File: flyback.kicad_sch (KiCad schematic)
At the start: 17 parts, among them Q1 IPD050N10N5, Q2 IPD050N10N5, T1 MSD1514-103ME

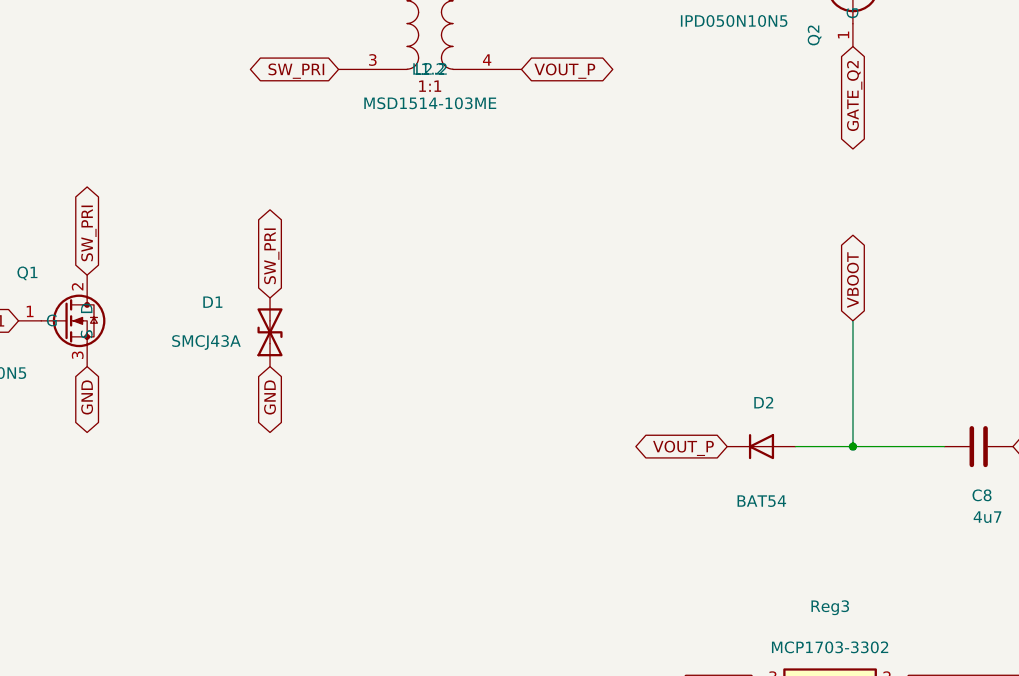
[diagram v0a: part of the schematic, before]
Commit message: Secondaire ISO7710+UCC27517 conservé, ajout retour Vout isolé AMC0311S, modèles 3D
- D2 (bootstrap) remplacé par BAT54C (cathode commune) pour compatibilité pinout
- AMC0311S (U7) ajouté : retour de mesure Vout isolé vers le connecteur C2000
- Connecteur Cpu1 étendu à 8 broches (signaux + masses)
- Correction pastilles Gate/Source sur l'empreinte custom TO-252 (pin1/pin3 inversées)
- Modèles 3D attachés aux empreintes custom (TO-252, MSD1514, A786MW V-chip)
- Image de rendu 3D ajoutée au README

Co-Authored-By: Claude Sonnet 5 <noreply@anthropic.com>
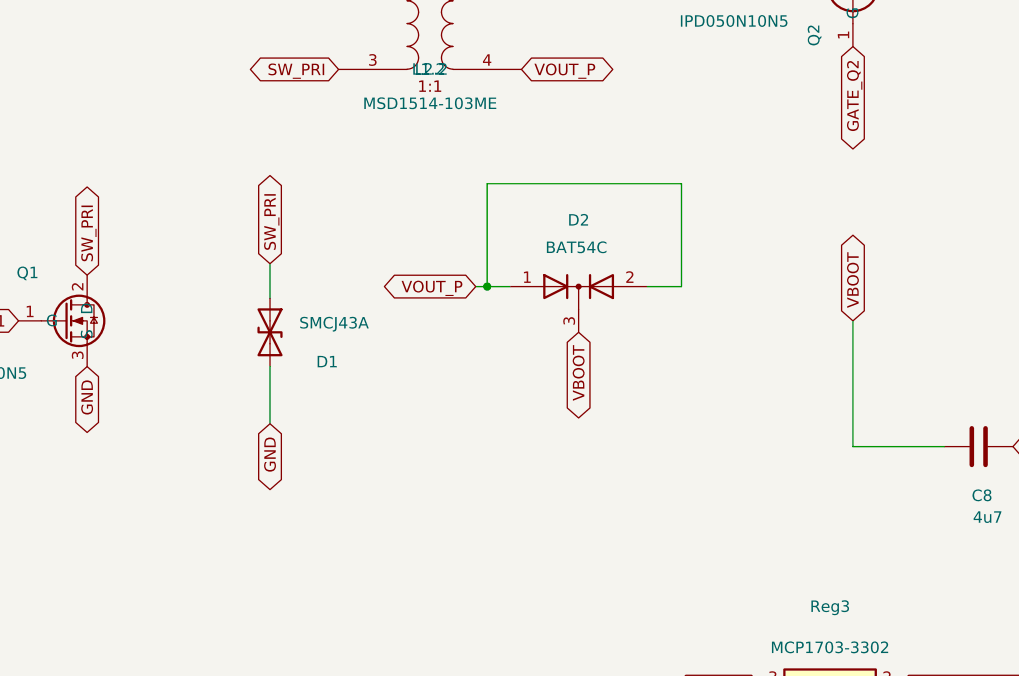
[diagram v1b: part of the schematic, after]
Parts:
- removed D2: BAT54, Diode_SMD:D_SOD-123, symbol Device:D
- added D2: BAT54C, Package_TO_SOT_SMD:SOT-23, symbol Device:D_Dual_CommonCathode_AAK
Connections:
- net GND: now also D1.2 (A2); no longer D1.1 (A1)
- net SW_PRI: now also D1.1 (A1); no longer D1.2 (A2)
- net VBOOT: now also D2.3 (K)
- net VOUT_P: now also D2.1 (A), D2.2 (A)
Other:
- moved on the sheet: D1

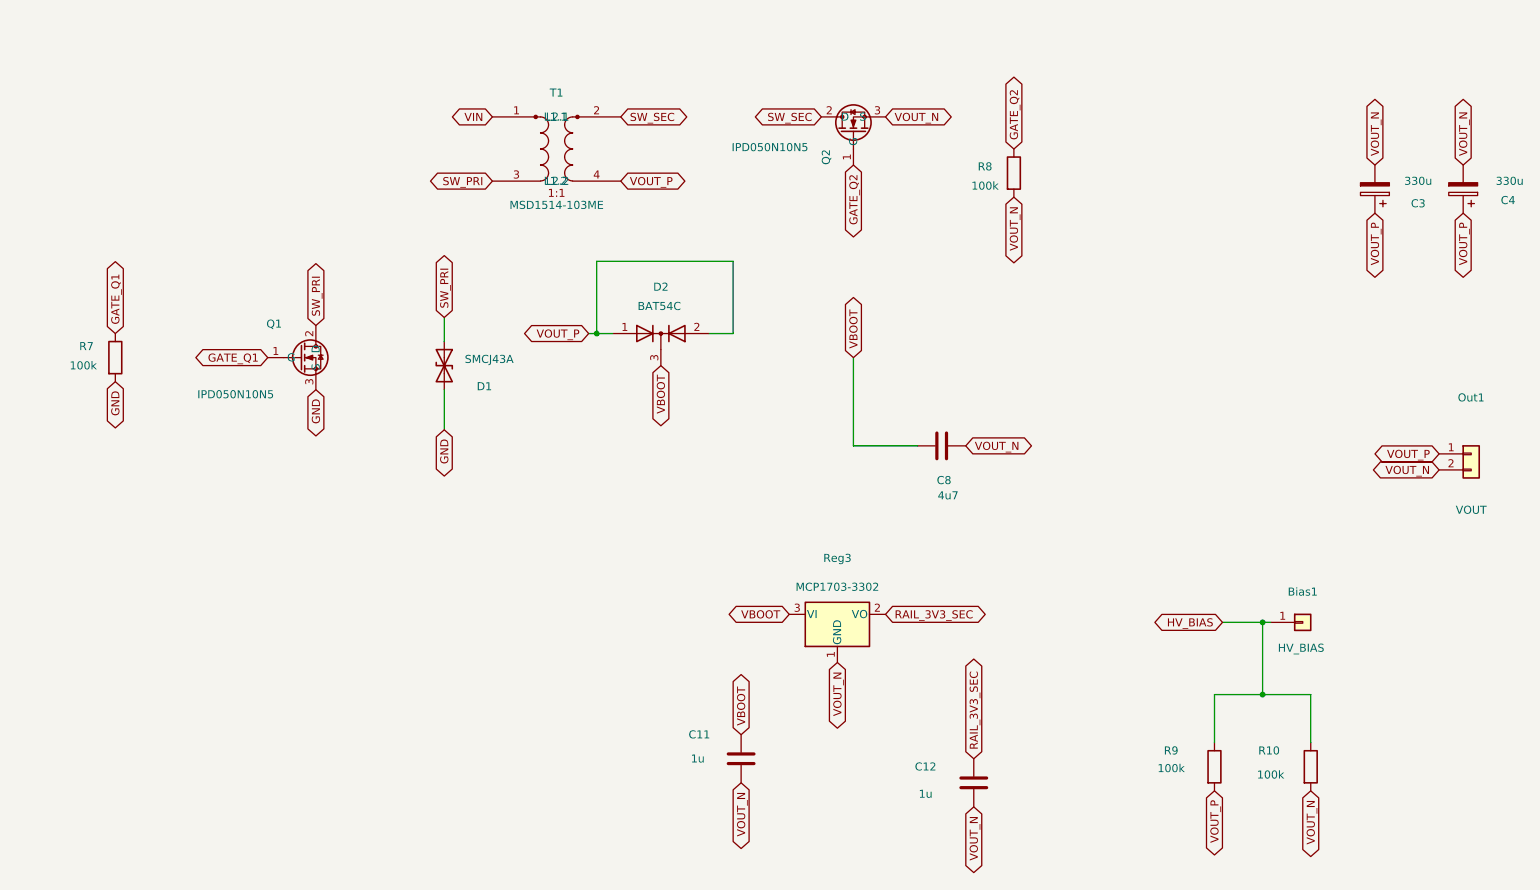
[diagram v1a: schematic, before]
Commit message: Isolation C2000 réelle (GND_CTRL/3V3_CTRL) + feuille Polarisation (HV_BIAS actif 0-90V)
- U3/U4/U5/U7/U8/U9 migrés côté contrôle vers GND_CTRL/3V3_CTRL (isolation
  du C2000 réellement effective, plus seulement nominale)
- Connecteurs CpuOut/CpuIn agrandis 2x04→2x08 (16 broches), marge pour
  futurs signaux et compatibilité avec d'autres cartes
- Nouvelle feuille polarisation.kicad_sch : pilotage actif de HV_BIAS
  (point de polarisation du secondaire flottant) depuis une alimentation
  400V externe — source de courant 300µA (BSS127I+MMBT2222), MOSFET
  variable BSS127I piloté par PWM isolé (ISO7710), protection TVS +
  pull-up grille, retour mesure isolé (AMC0311R)
- Nouveaux symboles custom BSS127I/MMBT2222, empreinte SOIC_DWV partagée
  par les amplis isolés de la famille AMC03x1R/AMC03x2R

Co-Authored-By: Claude Sonnet 5 <noreply@anthropic.com>
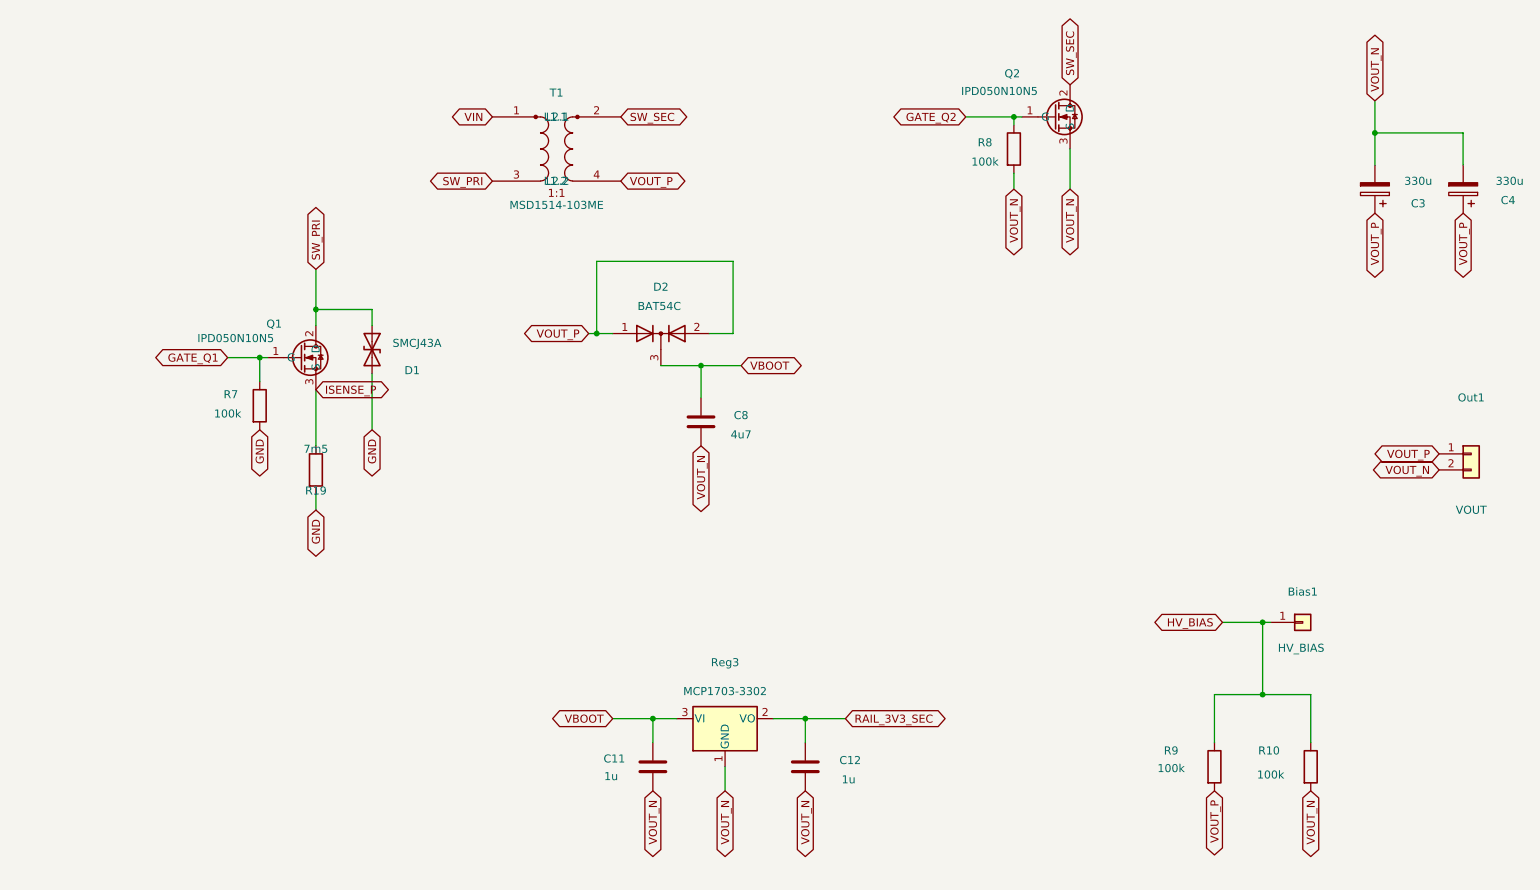
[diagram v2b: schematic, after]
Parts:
- added R19: 7m5, Resistor_SMD:R_1210_3225Metric, symbol Device:R
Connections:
- net GND: now also R19.2; no longer Q1.3 (S)
- new net ISENSE_P: Q1.3 (S), R19.1
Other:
- moved on the sheet: C11, C12, C8, D1, Q2, R7, R8, Reg3

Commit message: Retours temperature/courant primaire isoles, isolation C2000 reelle, feuille Polarisation finalisee (80V, R26 corrige par simulation)
- U8 (AMC0311R) : retour temperature primaire (thermistance NTC) isole
- U9 (AMC0302R) : retour courant primaire (shunt R19) isole
- Migration GND_CTRL/3V3_CTRL : le C2000 externe recoit ses propres nets
  d'alimentation/masse isoles (U3/U4/U5/U7/U8/U9), connecteurs CpuOut/CpuIn
  agrandis a 16 broches
- Feuille polarisation.kicad_sch reprise en etiquettes globales uniquement
  (plus de fils explicites) et alignee sur la grille 1.27mm
- Source de courant Q3/Q4/R25/R26 simplifiee a un rail fixe 80V (HV80_IN,
  ex-400V) ; R26 corrige de 2M7 a 75k apres simulation SPICE (ngspice,
  modeles reels Diodes Inc.) qui a revele que le montage se comporte
  comme une resistance plutot qu'une source plate - voir 00-intention-
  conception.md §15bis
- Nouveau script bom_family_report.py (remplace BOMconverter.py) :
  nomenclature groupee par famille, sans dependance externe, lit soit le
  netlist XML legacy d'Eeschema soit un CSV kicad-cli
- README.md : image du schema integree
- Mise a jour 00-intention-conception.md (§13-15bis)

Co-Authored-By: Claude Sonnet 5 <noreply@anthropic.com>
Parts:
- removed Bias1: HV_BIAS, Connector_PinHeader_2.54mm:PinHeader_1x01_P2.54mm_Vertical, symbol Connector_Generic:Conn_01x01
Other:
- moved on the sheet: D1

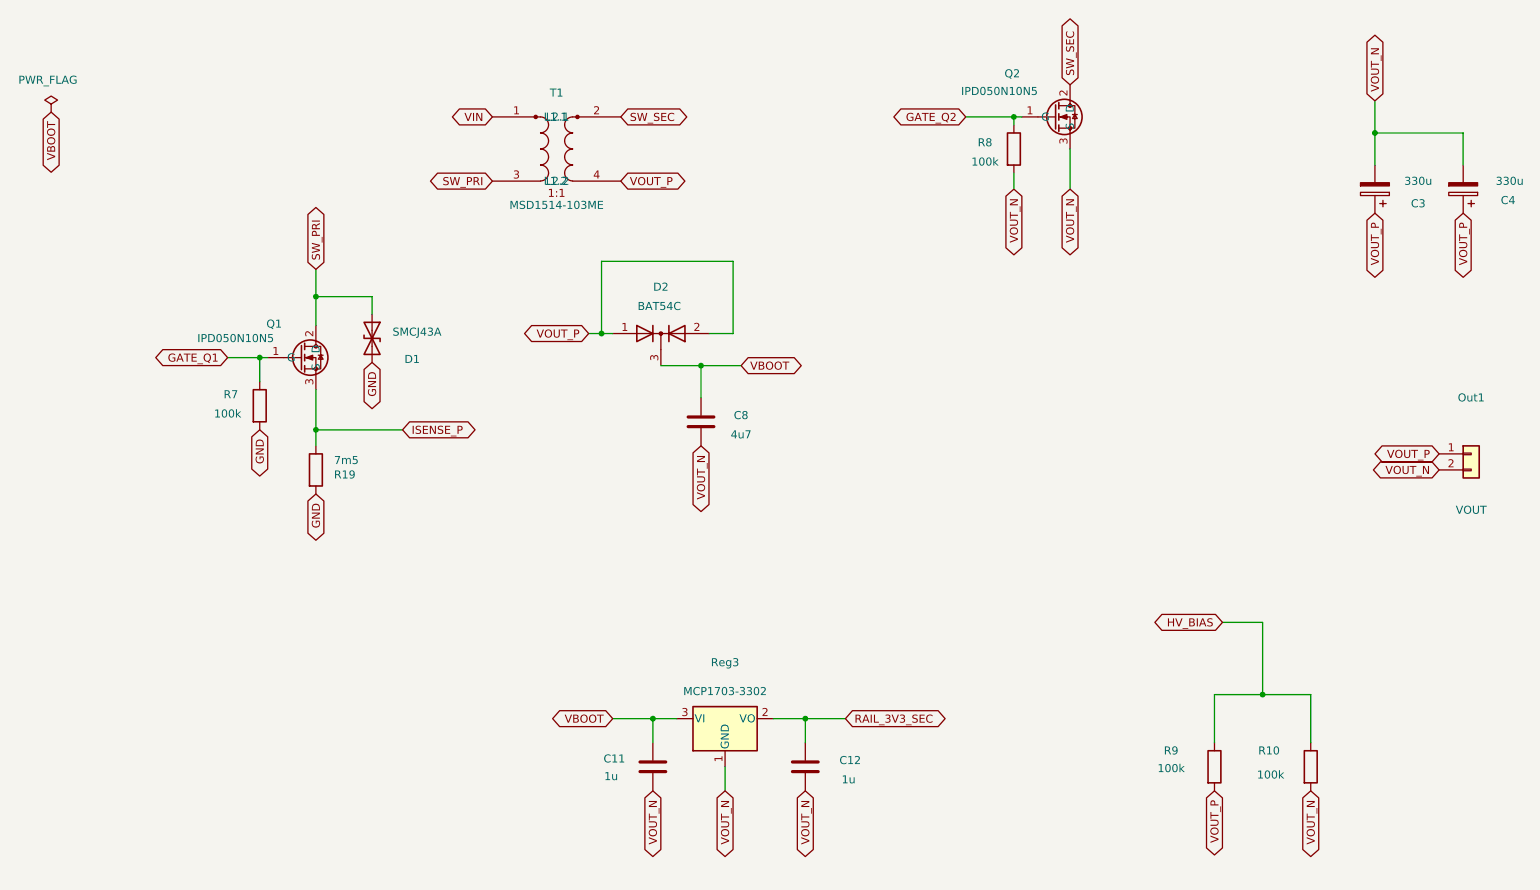
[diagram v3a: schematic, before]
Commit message: Validation 18,9W + redressement synchrone : UCC24612 (U12) remplace U2/U4, clamp D4 ajouté
Simulation SPICE à la cible réelle (18,9W, pas les 10W de validation initiale) :
Vds_Q2 dépasse 100V dès Vin=20V sans clamp secondaire, indépendamment du
redresseur. UCC24612 amène +5pts de rendement mais ne corrige pas la
surtension -- D4 (SMCJ54A) ajouté pour ça. U2/U4 retirés (timing firmware
aveugle, remplacé par la détection Vds de l'UCC24612).

Co-Authored-By: Claude Sonnet 5 <noreply@anthropic.com>
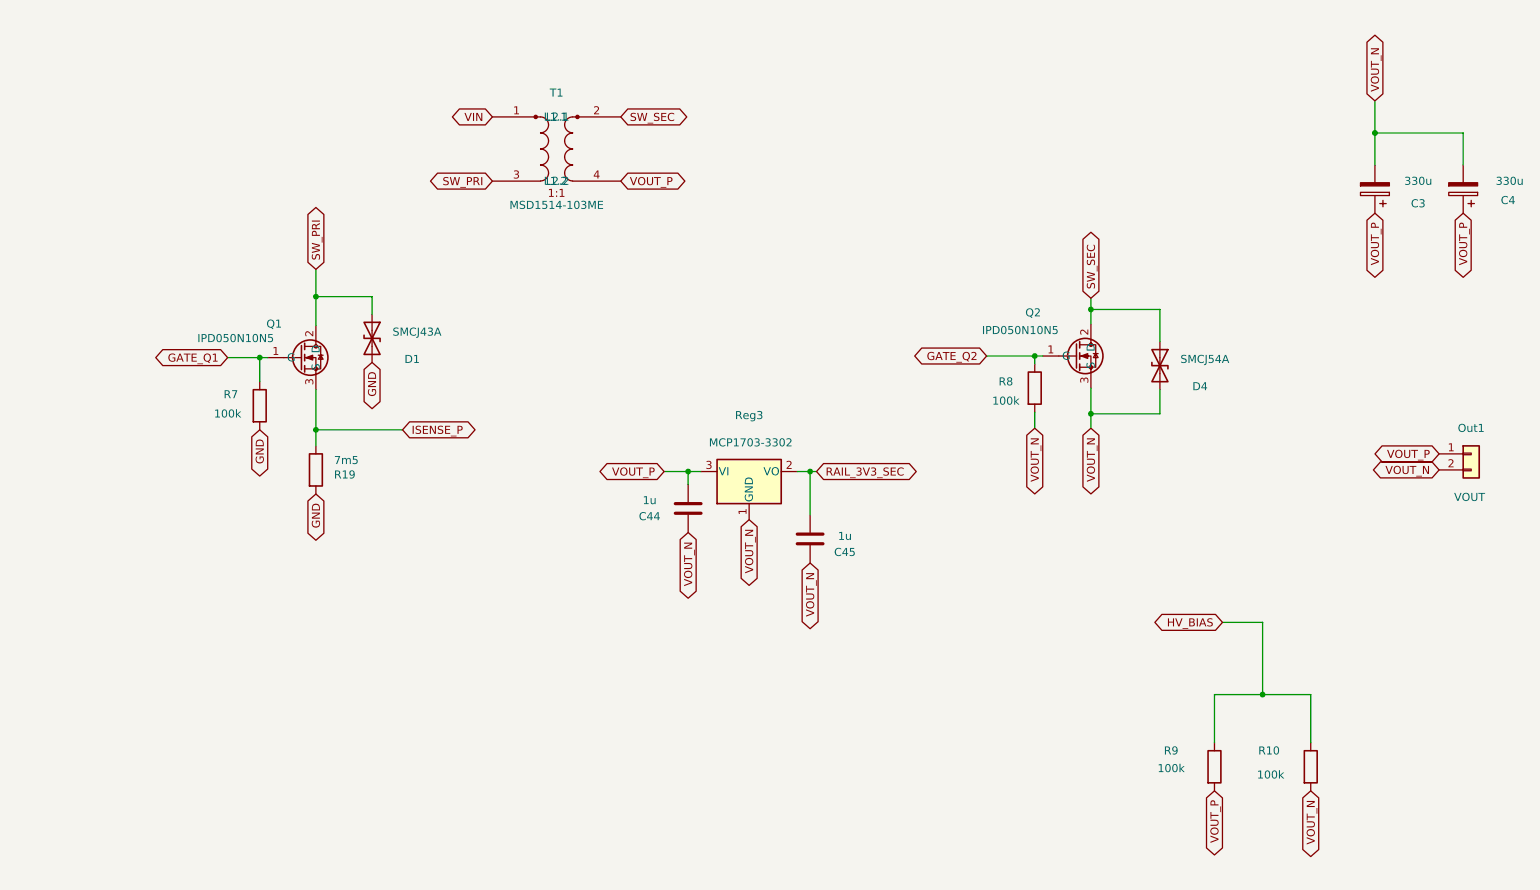
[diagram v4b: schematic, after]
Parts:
- removed C11, C12: 1u, Capacitor_SMD:C_0805_2012Metric, symbol Device:C
- removed C8: 4u7, Capacitor_SMD:C_0805_2012Metric, symbol Device:C
- removed D2: BAT54C, Package_TO_SOT_SMD:SOT-23, symbol Device:D_Dual_CommonCathode_AAK
- added C44, C45: 1u, Capacitor_SMD:C_0805_2012Metric, symbol Device:C
- added D4: SMCJ54A, Diode_SMD:D_SMC, symbol Device:D_TVS
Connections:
- net VBOOT is gone; now on net VOUT_P: Reg3.3 (VI)
- net RAIL_3V3_SEC: now also C45.1
- net SW_SEC: now also D4.1 (A1)
- net VOUT_N: now also C44.2, C45.2, D4.2 (A2)
- net VOUT_P: now also C44.1
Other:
- moved on the sheet: Q2, R8
